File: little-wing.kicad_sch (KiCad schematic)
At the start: 71 parts, among them IC1 AP7335-WG-7, J1 Conn_01x08, SW1 Power, SW2 Reset, U1 Nice_Nano_V2, U2 PMW3610

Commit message: Initial PCB layout
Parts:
- removed H1: NA_M4, local-libraries:MountingHole_3mm_Pad_Via, symbol Mechanical:MountingHole_Pad
- removed J1: Conn_01x08, Connector_PinHeader_2.54mm:PinHeader_1x06_P2.54mm_Vertical, symbol Connector_Generic:Conn_01x06
- removed R1: Battery, symbol ScottoKeebs:Placeholder_Resistor
- added J1: nice!view, Connector_Wire:SolderWire-0.1sqmm_1x05_P3.6mm_D0.4mm_OD1mm, symbol Connector:Conn_01x05_Socket
- added J2: Battery, Connector_JST:JST_PH_S2B-PH-K_1x02_P2.00mm_Horizontal, symbol Connector_Generic:Conn_01x02
- added J3, J4: trackball, Connector_Wire:SolderWire-0.1sqmm_1x06_P3.6mm_D0.4mm_OD1mm, symbol Connector:Conn_01x06_Socket
- C10, C11: footprint lib:C_0603_1608Metric -> Capacitor_SMD:C_0603_1608Metric
- D1, D10, D11, D12, D13, D14, D15, D16, D17, D2, D3, D4, D5, D6, D7, D8, D9: footprint (none) -> Diode_SMD:D_0603_1608Metric
- R2, R3: footprint lib:R_0603_1608Metric -> Resistor_SMD:R_0603_1608Metric
- S1, S10, S11, S12, S13, S14, S15, S16, S17, S2, S3, S4, S5, S6, S7, S8, S9: footprint (none) -> keyswitches:Kailh_socket_PG1350_reversible
- SW1: footprint (none) -> switch:switch-MSK-12C02-smd
- SW2: footprint (none) -> ScottoKeebs_Components:Button_MJTP1243
- U1: value Nice_Nano_V2 -> nice!nano v2; footprint ScottoKeebs_MCU:Nice_Nano_V2 -> keyboard_reversible:ProMicro
- U2: footprint mylib:PMW3610 -> sensor:PMW3610
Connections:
- net Col 0: now also U1.18 (19); no longer U1.7 (4)
- net Col 1: now also U1.17 (18); no longer U1.8 (5)
- net Col 2: now also U1.16 (15); no longer U1.9 (6)
- net Col 3: now also U1.15 (14); no longer U1.10 (7)
- net Col 4: now also U1.14 (16); no longer U1.11 (8)
- net Col 5: now also U1.13 (10); no longer U1.12 (9)
- net GND: now also J1.4 (Pin_4), J2.1 (Pin_1), J3.6 (Pin_6), J4.6 (Pin_6)
- net RGB: now also U1.8 (5); no longer U1.2 (0)
- net Row 0: now also U1.10 (7); no longer U1.15 (14)
- net Row 1: now also U1.11 (8); no longer U1.14 (16)
- net Row 2: now also U1.12 (9); no longer U1.13 (10)
- net VCC: now also J1.3 (Pin_3), J4.1 (Pin_1); no longer C11.1, C7.1, IC1.1 (IN), IC1.3 (EN), R1.2, U2.6 (VDDIO)
- net CS_D: now reaches U1.1
- net CS_D: now also J1.5 (Pin_5)
- net SCK: now reaches U1.5 (2)
- net SCK: now also J1.2 (Pin_2), J4.4 (Pin_4)
- net MOSI: now reaches U1.6 (3)
- net MOSI: now also J1.1 (Pin_1), J4.3 (Pin_3)
- net at SW1.1: now also J2.2 (Pin_2)
- net MOTION_2 renamed MOTION
- net MOTION: now also J3.5 (Pin_5)
- net NCS_2 renamed NCS
- net NCS: now also J3.2 (Pin_2)
- net SCLK_2 renamed SCLK
- net SCLK: now also J3.4 (Pin_4)
- net SDIO_2 renamed SDIO
- net SDIO: now also J3.3 (Pin_3)
- new net 3.3v: C11.1, C7.1, IC1.1 (IN), IC1.3 (EN), J3.1 (Pin_1), R1.2, U2.6 (VDDIO)
- new net CS_T: J4.2 (Pin_2), U1.2 (0)
- new net MISO: J4.5 (Pin_5), U1.7 (4)

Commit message: Flipping the components in place
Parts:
- D1, D10, D11, D12, D13, D14, D15, D16, D17, D2, D3, D4, D5, D6, D7, D8, D9: footprint Diode_SMD:D_0603_1608Metric -> ScottoKeebs_Components:Diode_SOD-123
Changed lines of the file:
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@@
 			)
 		)
-		(property "Footprint" "Diode_SMD:D_0603_1608Metric"
+		(property "Footprint" "ScottoKeebs_Components:Diode_SOD-123"
 			(at 203.2 67.31 0)
 			(effects
@@
 			)
 		)
-		(property "Footprint" "Diode_SMD:D_0603_1608Metric"
+		(property "Footprint" "ScottoKeebs_Components:Diode_SOD-123"
 			(at 259.08 67.31 0)
 			(effects
@@
 			)
 		)
-		(property "Footprint" "Diode_SMD:D_0603_1608Metric"
+		(property "Footprint" "ScottoKeebs_Components:Diode_SOD-123"
 			(at 217.17 85.09 0)
 			(effects
@@
 			)
 		)
-		(property "Footprint" "Diode_SMD:D_0603_1608Metric"
+		(property "Footprint" "ScottoKeebs_Components:Diode_SOD-123"
 			(at 259.08 48.26 0)
 			(effects
@@
 			)
 		)
-		(property "Footprint" "Diode_SMD:D_0603_1608Metric"
+		(property "Footprint" "ScottoKeebs_Components:Diode_SOD-123"
 			(at 273.05 48.26 0)
 			(effects
@@
 			)
 		)
-		(property "Footprint" "Diode_SMD:D_0603_1608Metric"
+		(property "Footprint" "ScottoKeebs_Components:Diode_SOD-123"
 			(at 231.14 67.31 0)
 			(effects
@@
 			)
 		)
-		(property "Footprint" "Diode_SMD:D_0603_1608Metric"
+		(property "Footprint" "ScottoKeebs_Components:Diode_SOD-123"
 			(at 259.08 85.09 0)
 			(effects
@@
 			)
 		)
-		(property "Footprint" "Diode_SMD:D_0603_1608Metric"
+		(property "Footprint" "ScottoKeebs_Components:Diode_SOD-123"
 			(at 245.11 85.09 0)
 			(effects
@@
 			)
 		)
-		(property "Footprint" "Diode_SMD:D_0603_1608Metric"
+		(property "Footprint" "ScottoKeebs_Components:Diode_SOD-123"
 			(at 203.2 85.09 0)
 			(effects
@@
 			)
 		)
-		(property "Footprint" "Diode_SMD:D_0603_1608Metric"
+		(property "Footprint" "ScottoKeebs_Components:Diode_SOD-123"
 			(at 245.11 67.31 0)
 			(effects
@@
 			)
 		)
-		(property "Footprint" "Diode_SMD:D_0603_1608Metric"
+		(property "Footprint" "ScottoKeebs_Components:Diode_SOD-123"
 			(at 203.2 48.26 0)
 			(effects
@@
 			)
 		)
-		(property "Footprint" "Diode_SMD:D_0603_1608Metric"
+		(property "Footprint" "ScottoKeebs_Components:Diode_SOD-123"
 			(at 217.17 67.31 0)
 			(effects
@@
 			)
 		)
-		(property "Footprint" "Diode_SMD:D_0603_1608Metric"
+		(property "Footprint" "ScottoKeebs_Components:Diode_SOD-123"
 			(at 245.11 48.26 0)
 			(effects
@@
 			)
 		)
-		(property "Footprint" "Diode_SMD:D_0603_1608Metric"
+		(property "Footprint" "ScottoKeebs_Components:Diode_SOD-123"
 			(at 231.14 85.09 0)
 			(effects
@@
 			)
 		)
-		(property "Footprint" "Diode_SMD:D_0603_1608Metric"
+		(property "Footprint" "ScottoKeebs_Components:Diode_SOD-123"
 			(at 273.05 67.31 0)
 			(effects
@@
 			)
 		)
-		(property "Footprint" "Diode_SMD:D_0603_1608Metric"
+		(property "Footprint" "ScottoKeebs_Components:Diode_SOD-123"
 			(at 217.17 48.26 0)
 			(effects
@@
 			)
 		)
-		(property "Footprint" "Diode_SMD:D_0603_1608Metric"
+		(property "Footprint" "ScottoKeebs_Components:Diode_SOD-123"
 			(at 231.14 48.26 0)
 			(effects

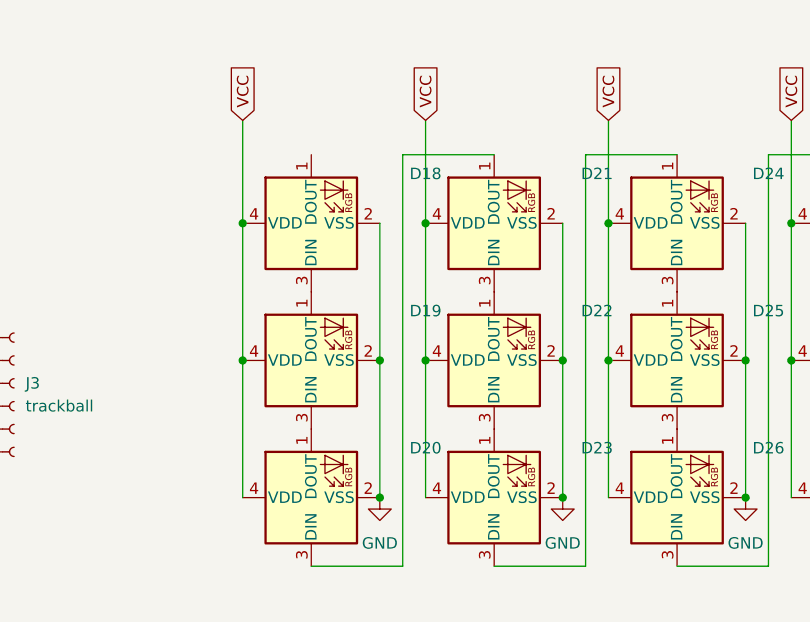
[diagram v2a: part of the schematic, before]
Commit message: Remaking the PCB for better alignment
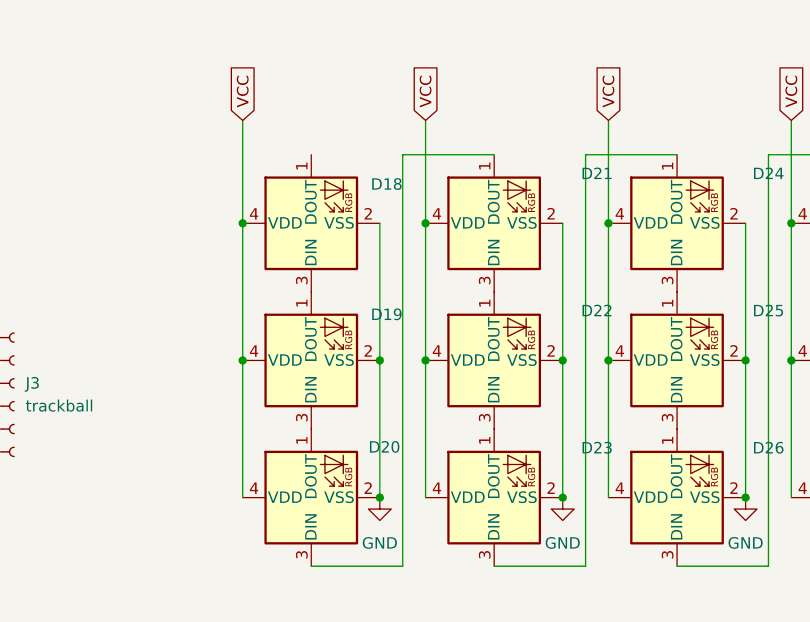
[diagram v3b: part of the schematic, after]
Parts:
- D1, D10, D11, D12, D13, D14, D15, D16, D17, D2, D3, D4, D5, D6, D7, D8, D9: footprint ScottoKeebs_Components:Diode_SOD-123 -> ScottoKeebs_Components:Diode_SOD-123_Reversible
- D18, D19, D20, D21, D22, D23, D24, D25, D26, D27, D28, D29, D30, D31, D32, D33, D34: footprint ScottoKeebs_Components:LED_SK6812MINI -> ScottoKeebs_Components:LED_SK6812MINI_Reversible
- J1: footprint Connector_Wire:SolderWire-0.1sqmm_1x05_P3.6mm_D0.4mm_OD1mm -> Connector_PinHeader_2.54mm:PinHeader_1x05_P2.54mm_Vertical
- J2: footprint Connector_JST:JST_PH_S2B-PH-K_1x02_P2.00mm_Horizontal -> Connector_JST:JST_ZH_S2B-ZR-SM4A-TF_1x02-1MP_P1.50mm_Horizontal_Reversible
- J3, J4: footprint Connector_Wire:SolderWire-0.1sqmm_1x06_P3.6mm_D0.4mm_OD1mm -> Connector_Wuerth:Wuerth_WR-WTB_64800611622_1x06_P1.50mm_Vertical
- S1, S10, S11, S12, S13, S14, S15, S16, S17, S2, S3, S4, S5, S6, S7, S8, S9: footprint keyswitches:Kailh_socket_PG1350_reversible -> keyswitches:Kailh_socket_PG1350_reversible_better
- SW1: footprint switch:switch-MSK-12C02-smd -> Button_Switch_SMD:SW_SPDT_PCM12_Reversible
- SW2: footprint ScottoKeebs_Components:Button_MJTP1243 -> Button_Switch_SMD:SW_SPST_B3U-1000P_Reversible

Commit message: Making a column work
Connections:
- net GND: now also D18.3 (GND), D19.3 (GND), D20.3 (GND), D21.3 (GND), D22.3 (GND), D23.3 (GND), D24.3 (GND), D25.3 (GND), D26.3 (GND), D27.3 (GND), D28.3 (GND), D29.3 (GND), D30.3 (GND), D31.3 (GND), D32.3 (GND), D33.3 (GND), D34.3 (GND); no longer D18.2 (VSS), D19.2 (VSS), D20.2 (VSS), D21.2 (VSS), D22.2 (VSS), D23.2 (VSS), D24.2 (VSS), D25.2 (VSS), D26.2 (VSS), D27.2 (VSS), D28.2 (VSS), D29.2 (VSS), D30.2 (VSS), D31.2 (VSS), D32.2 (VSS), D33.2 (VSS), D34.2 (VSS)
- net RGB: now also D34.4 (DIN); no longer D34.3 (DIN)
- net VCC: now also D18.1 (VSS), D19.1 (VSS), D20.1 (VSS), D21.1 (VSS), D22.1 (VSS), D23.1 (VSS), D24.1 (VSS), D25.1 (VSS), D26.1 (VSS), D27.1 (VSS), D28.1 (VSS), D29.1 (VSS), D30.1 (VSS), D31.1 (VSS), D32.1 (VSS), D33.1 (VSS), D34.1 (VSS); no longer D18.4 (VDD), D19.4 (VDD), D20.4 (VDD), D21.4 (VDD), D22.4 (VDD), D23.4 (VDD), D24.4 (VDD), D25.4 (VDD), D26.4 (VDD), D27.4 (VDD), D28.4 (VDD), D29.4 (VDD), D30.4 (VDD), D31.4 (VDD), D32.4 (VDD), D33.4 (VDD), D34.4 (VDD)
- new net: D31.4 (DIN), D32.2 (DOUT)
- new net: D32.4 (DIN), D33.2 (DOUT)
- new net: D28.4 (DIN), D29.2 (DOUT)
- new net: D29.4 (DIN), D30.2 (DOUT)
- new net: D19.4 (DIN), D20.2 (DOUT)
- new net: D20.4 (DIN), D21.2 (DOUT)
- new net: D23.4 (DIN), D24.2 (DOUT)
- new net: D24.4 (DIN), D25.2 (DOUT)
- new net: D22.4 (DIN), D23.2 (DOUT)
- new net: D25.4 (DIN), D26.2 (DOUT)
- new net: D21.4 (DIN), D22.2 (DOUT)
- new net: D30.4 (DIN), D31.2 (DOUT)
- new net: D18.4 (DIN), D19.2 (DOUT)
- new net: D27.4 (DIN), D28.2 (DOUT)
- new net: D26.4 (DIN), D27.2 (DOUT)
- new net: D33.4 (DIN), D34.2 (DOUT)
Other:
- moved on the sheet: D18, D19, D20, D21, D22, D23, D24, D25, D26, D27, D28, D29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

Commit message: Saving the main lanes progress
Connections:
- net Col 0: now also S13.1, S14.1, S15.1; no longer S1.1, S2.1, S3.1
- net Col 1: now also S10.1, S11.1, S12.1; no longer S4.1, S5.1, S6.1
- net Col 3: now also S4.1, S5.1, S6.1; no longer S10.1, S11.1, S12.1
- net Col 4: now also S1.1, S2.1, S3.1; no longer S13.1, S14.1, S15.1

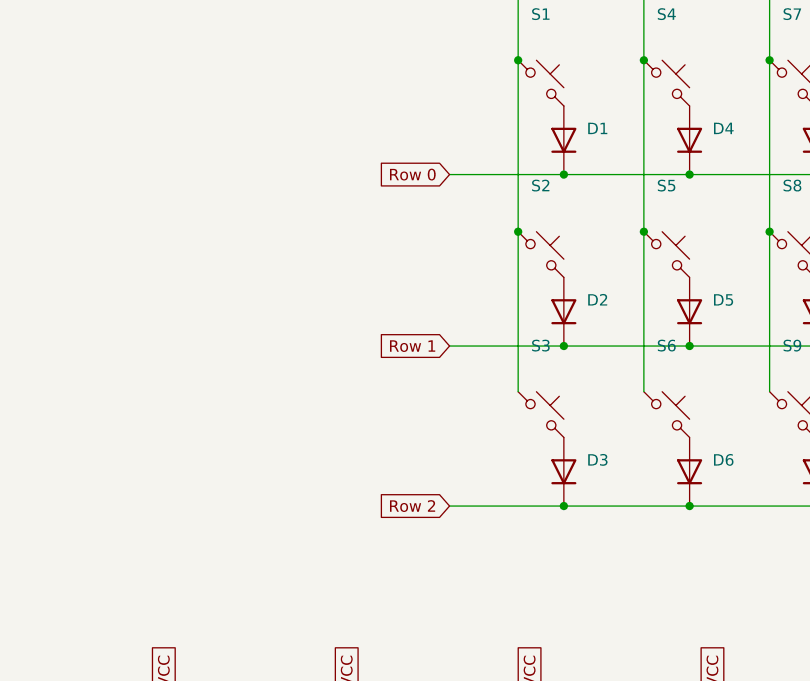
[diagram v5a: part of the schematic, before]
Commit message: Initial alignment of the sensor block
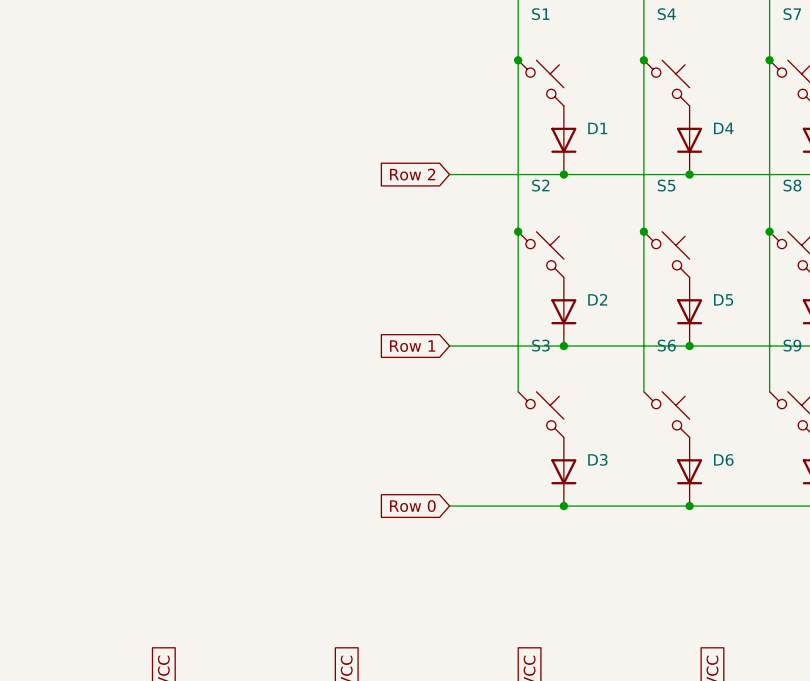
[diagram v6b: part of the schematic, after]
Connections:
- net Row 0: now also D12.1 (K), D15.1 (K), D3.1 (K), D6.1 (K), D9.1 (K); no longer D1.1 (K), D10.1 (K), D13.1 (K), D16.1 (K), D4.1 (K), D7.1 (K)
- net Row 2: now also D1.1 (K), D10.1 (K), D13.1 (K), D16.1 (K), D4.1 (K), D7.1 (K); no longer D12.1 (K), D15.1 (K), D3.1 (K), D6.1 (K), D9.1 (K)

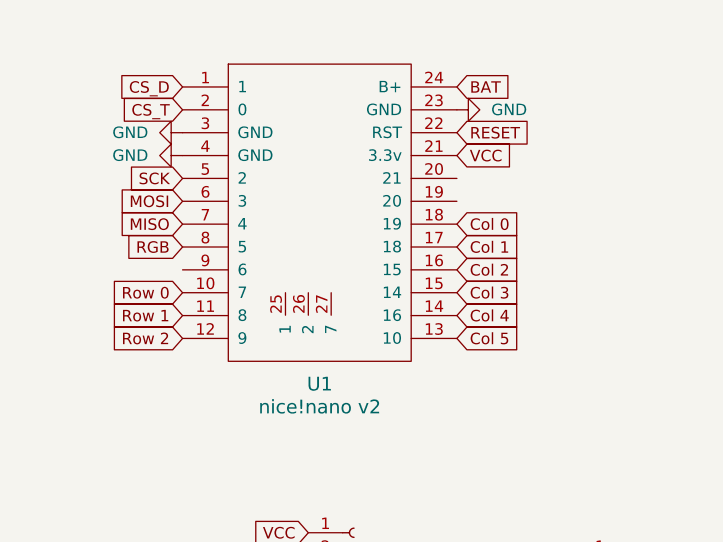
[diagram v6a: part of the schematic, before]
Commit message: Rounding out the main columns cutouts
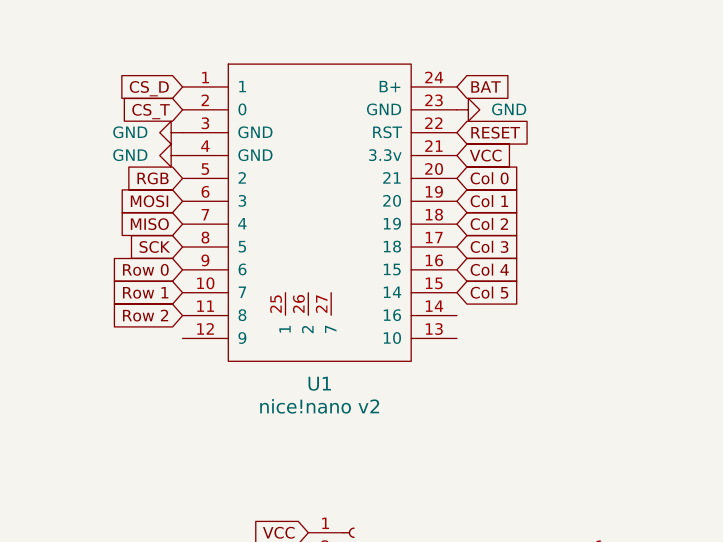
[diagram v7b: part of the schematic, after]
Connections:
- net Col 0: now also U1.20 (21); no longer U1.18 (19)
- net Col 1: now also U1.19 (20); no longer U1.17 (18)
- net Col 2: now also U1.18 (19); no longer U1.16 (15)
- net Col 3: now also U1.17 (18); no longer U1.15 (14)
- net Col 4: now also U1.16 (15); no longer U1.14 (16)
- net Col 5: now also U1.15 (14); no longer U1.13 (10)
- net RGB: now also U1.5 (2); no longer U1.8 (5)
- net Row 0: now also U1.9 (6); no longer U1.10 (7)
- net Row 1: now also U1.10 (7); no longer U1.11 (8)
- net Row 2: now also U1.11 (8); no longer U1.12 (9)
- net SCK: now also U1.8 (5); no longer U1.5 (2)

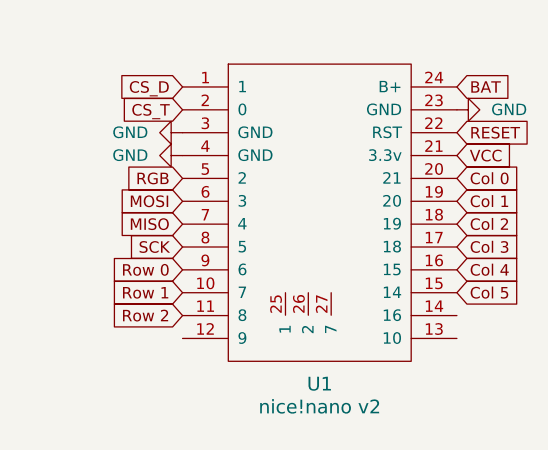
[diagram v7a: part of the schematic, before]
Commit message: Initial MCU wiring
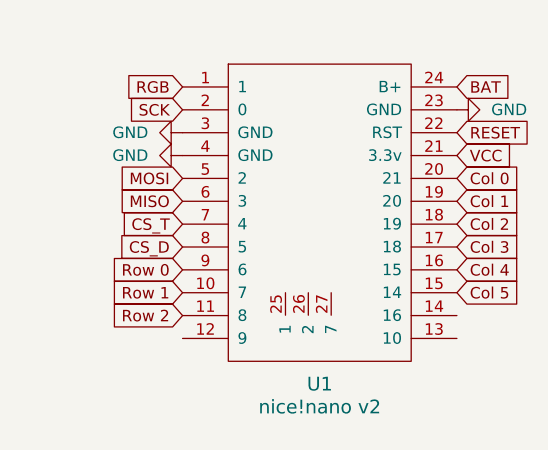
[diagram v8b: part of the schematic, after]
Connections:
- net CS_D: now also U1.8 (5); no longer U1.1
- net CS_T: now also U1.7 (4); no longer U1.2 (0)
- net MISO: now also U1.6 (3); no longer U1.7 (4)
- net MOSI: now also U1.5 (2); no longer U1.6 (3)
- net RGB: now also U1.1; no longer U1.5 (2)
- net SCK: now also U1.2 (0); no longer U1.8 (5)
